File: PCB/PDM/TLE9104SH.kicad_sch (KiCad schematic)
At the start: 15 parts

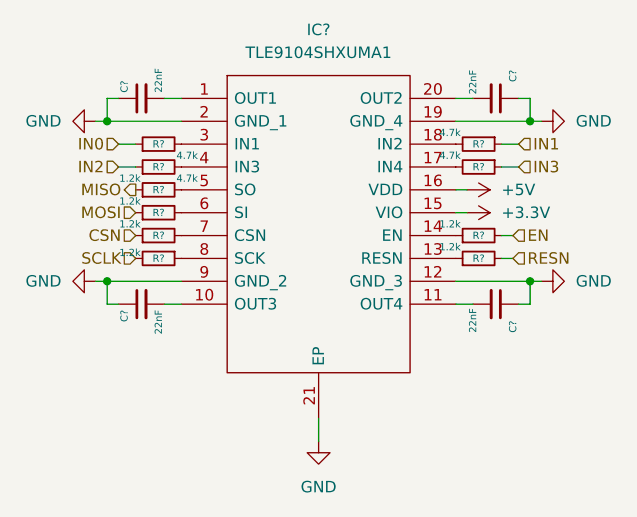
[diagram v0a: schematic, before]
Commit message: Concept revision and MCU section changes
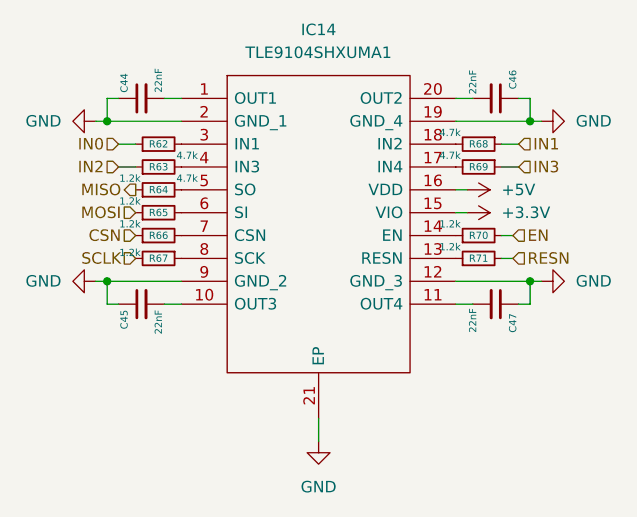
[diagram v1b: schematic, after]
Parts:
- IC14: renamed from IC?; footprint SOP50P1030X260-21N -> PDM_Additional:SOP50P1030X260-21N
- gave numbers to parts that had none: 14
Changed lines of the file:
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@@
   (symbol (lib_id "power:GND") (at 40.005 63.5 270) (mirror x) (unit 1)
     (in_bom yes) (on_board yes) (fields_autoplaced)
-    (property "Reference" "#PWR?" (id 0) (at 33.655 63.5 0)
+    (property "Reference" "#PWR0175" (id 0) (at 33.655 63.5 0)
       (effects (font (size 1.27 1.27)) hide)
     )
@@
   (symbol (lib_id "Device:R_Small") (at 82.55 48.26 270) (unit 1)
     (in_bom yes) (on_board yes)
-    (property "Reference" "R?" (id 0) (at 82.55 48.26 90)
+    (property "Reference" "R68" (id 0) (at 82.55 48.26 90)
       (effects (font (size 0.8 0.8)))
     )
@@
   (symbol (lib_id "power:+5V") (at 81.28 53.34 270) (unit 1)
     (in_bom yes) (on_board yes) (fields_autoplaced)
-    (property "Reference" "#PWR?" (id 0) (at 77.47 53.34 0)
+    (property "Reference" "#PWR0170" (id 0) (at 77.47 53.34 0)
       (effects (font (size 1.27 1.27)) hide)
     )
@@
   (symbol (lib_id "power:GND") (at 89.535 63.5 90) (mirror x) (unit 1)
     (in_bom yes) (on_board yes) (fields_autoplaced)
-    (property "Reference" "#PWR?" (id 0) (at 95.885 63.5 0)
+    (property "Reference" "#PWR0172" (id 0) (at 95.885 63.5 0)
       (effects (font (size 1.27 1.27)) hide)
     )
@@
   (symbol (lib_id "Device:R_Small") (at 82.55 58.42 90) (unit 1)
     (in_bom yes) (on_board yes)
-    (property "Reference" "R?" (id 0) (at 82.55 58.42 90)
+    (property "Reference" "R70" (id 0) (at 82.55 58.42 90)
       (effects (font (size 0.8 0.8)))
     )
@@
   (symbol (lib_id "Device:C_Small") (at 45.085 43.18 90) (unit 1)
     (in_bom yes) (on_board yes)
-    (property "Reference" "C?" (id 0) (at 43.18 42.545 0)
+    (property "Reference" "C44" (id 0) (at 43.18 42.545 0)
       (effects (font (size 0.8 0.8)) (justify left))
     )
@@
   (symbol (lib_id "Device:R_Small") (at 46.99 55.88 90) (unit 1)
     (in_bom yes) (on_board yes)
-    (property "Reference" "R?" (id 0) (at 46.99 55.88 90)
+    (property "Reference" "R65" (id 0) (at 46.99 55.88 90)
       (effects (font (size 0.8 0.8)))
     )
@@
   (symbol (lib_id "Device:R_Small") (at 46.99 58.42 90) (unit 1)
     (in_bom yes) (on_board yes)
-    (property "Reference" "R?" (id 0) (at 46.99 58.42 90)
+    (property "Reference" "R66" (id 0) (at 46.99 58.42 90)
       (effects (font (size 0.8 0.8)))
     )
@@
   (symbol (lib_id "Device:R_Small") (at 46.99 53.34 90) (unit 1)
     (in_bom yes) (on_board yes)
-    (property "Reference" "R?" (id 0) (at 46.99 53.34 90)
+    (property "Reference" "R64" (id 0) (at 46.99 53.34 90)
       (effects (font (size 0.8 0.8)))
     )
@@
   (symbol (lib_id "power:GND") (at 64.77 81.28 0) (unit 1)
     (in_bom yes) (on_board yes) (fields_autoplaced)
-    (property "Reference" "#PWR?" (id 0) (at 64.77 87.63 0)
+    (property "Reference" "#PWR0174" (id 0) (at 64.77 87.63 0)
       (effects (font (size 1.27 1.27)) hide)
     )
@@
   (symbol (lib_id "Device:C_Small") (at 45.085 66.04 90) (mirror x) (unit 1)
     (in_bom yes) (on_board yes)
-    (property "Reference" "C?" (id 0) (at 43.18 66.675 0)
+    (property "Reference" "C45" (id 0) (at 43.18 66.675 0)
       (effects (font (size 0.8 0.8)) (justify left))
     )
@@
   (symbol (lib_id "PDM_additional:TLE9104SHXUMA1") (at 49.53 43.18 0) (unit 1)
     (in_bom yes) (on_board yes) (fields_autoplaced)
-    (property "Reference" "IC?" (id 0) (at 64.77 35.56 0))
+    (property "Reference" "IC14" (id 0) (at 64.77 35.56 0))
     (property "Value" "TLE9104SHXUMA1" (id 1) (at 64.77 38.1 0))
-    (property "Footprint" "SOP50P1030X260-21N" (id 2) (at 76.2 40.64 0)
+    (property "Footprint" "PDM_Additional:SOP50P1030X260-21N" (id 2) (at 76.2 40.64 0)
       (effects (font (size 1.27 1.27)) (justify left) hide)
     )
@@
   (symbol (lib_id "Device:R_Small") (at 82.55 60.96 90) (unit 1)
     (in_bom yes) (on_board yes)
-    (property "Reference" "R?" (id 0) (at 82.55 60.96 90)
+    (property "Reference" "R71" (id 0) (at 82.55 60.96 90)
       (effects (font (size 0.8 0.8)))
     )
@@
   (symbol (lib_id "power:GND") (at 40.005 45.72 270) (unit 1)
     (in_bom yes) (on_board yes) (fields_autoplaced)
-    (property "Reference" "#PWR?" (id 0) (at 33.655 45.72 0)
+    (property "Reference" "#PWR0173" (id 0) (at 33.655 45.72 0)
       (effects (font (size 1.27 1.27)) hide)
     )
@@
   (symbol (lib_id "power:GND") (at 89.535 45.72 90) (unit 1)
     (in_bom yes) (on_board yes) (fields_autoplaced)
-    (property "Reference" "#PWR?" (id 0) (at 95.885 45.72 0)
+    (property "Reference" "#PWR0107" (id 0) (at 95.885 45.72 0)
       (effects (font (size 1.27 1.27)) hide)
     )
@@
   (symbol (lib_id "Device:R_Small") (at 46.99 48.26 90) (unit 1)
     (in_bom yes) (on_board yes)
-    (property "Reference" "R?" (id 0) (at 46.99 48.26 90)
+    (property "Reference" "R62" (id 0) (at 46.99 48.26 90)
       (effects (font (size 0.8 0.8)))
     )
@@
   (symbol (lib_id "Device:R_Small") (at 82.55 50.8 270) (unit 1)
     (in_bom yes) (on_board yes)
-    (property "Reference" "R?" (id 0) (at 82.55 50.8 90)
+    (property "Reference" "R69" (id 0) (at 82.55 50.8 90)
       (effects (font (size 0.8 0.8)))
     )
@@
   (symbol (lib_id "Device:R_Small") (at 46.99 50.8 90) (unit 1)
     (in_bom yes) (on_board yes)
-    (property "Reference" "R?" (id 0) (at 46.99 50.8 90)
+    (property "Reference" "R63" (id 0) (at 46.99 50.8 90)
       (effects (font (size 0.8 0.8)))
     )
@@
   (symbol (lib_id "Device:C_Small") (at 84.455 43.18 270) (unit 1)
     (in_bom yes) (on_board yes)
-    (property "Reference" "C?" (id 0) (at 86.36 40.005 0)
+    (property "Reference" "C46" (id 0) (at 86.36 40.005 0)
       (effects (font (size 0.8 0.8)) (justify left))
     )
@@
   (symbol (lib_id "power:+3.3V") (at 81.28 55.88 270) (unit 1)
     (in_bom yes) (on_board yes) (fields_autoplaced)
-    (property "Reference" "#PWR?" (id 0) (at 77.47 55.88 0)
+    (property "Reference" "#PWR0171" (id 0) (at 77.47 55.88 0)
       (effects (font (size 1.27 1.27)) hide)
     )
@@
   (symbol (lib_id "Device:C_Small") (at 84.455 66.04 270) (mirror x) (unit 1)
     (in_bom yes) (on_board yes)
-    (property "Reference" "C?" (id 0) (at 86.36 69.215 0)
+    (property "Reference" "C47" (id 0) (at 86.36 69.215 0)
       (effects (font (size 0.8 0.8)) (justify left))
     )
@@
   (symbol (lib_id "Device:R_Small") (at 46.99 60.96 270) (unit 1)
     (in_bom yes) (on_board yes)
-    (property "Reference" "R?" (id 0) (at 46.99 60.96 90)
-      (effects (font (size 0.8 0.8)))
-    )
+    (property "Reference" "R67" (id 0) (at 46.99 60.96 90)
+      (effects (font (size 0.8 0.8)))
+    )
